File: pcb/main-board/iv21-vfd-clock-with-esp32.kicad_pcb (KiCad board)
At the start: 2 copper layers, 101.5 x 40 mm, 29 parts, among them J1 Conn_02x10_Odd_Even, J2 4328, P1 USB_C_Plug_USB2.0, SW1 SW_SPST, SW2 SW_SPST, U1 MAX6921AQI_, U2 MOUDLE-SEEEDUINO-XIAO-ESP32C3, U3 AP3012, U4 S-1167B24-M5T

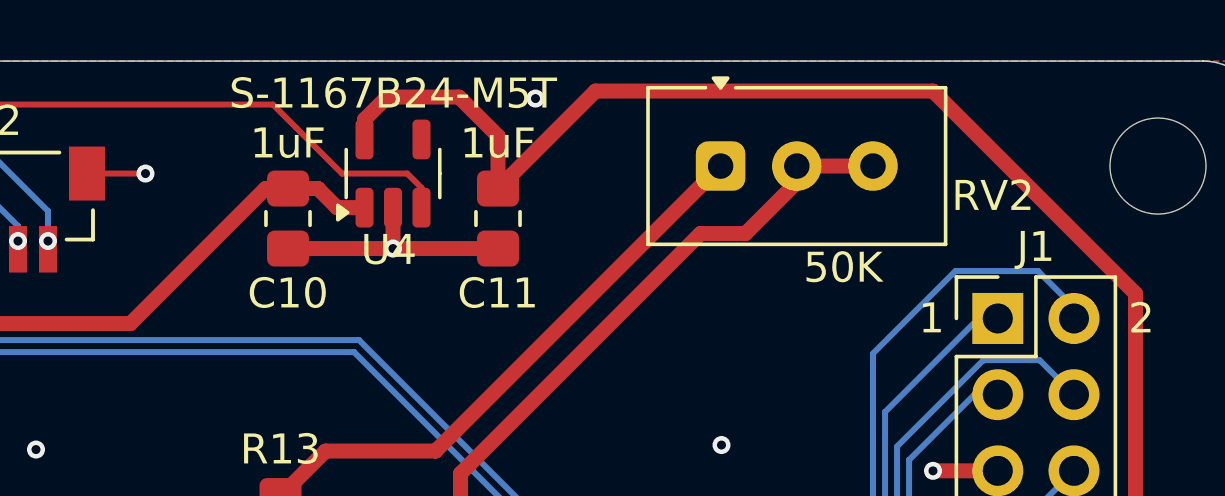
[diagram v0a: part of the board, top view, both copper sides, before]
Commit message: Fix some silkmask labels for trim pot.
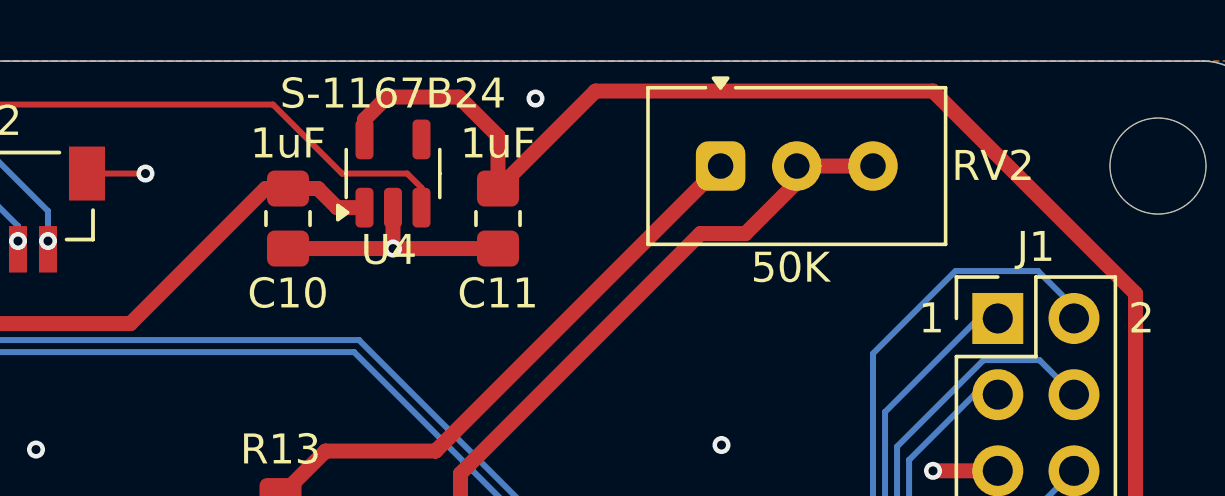
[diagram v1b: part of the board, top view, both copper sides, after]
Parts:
- U4: value S-1167B24-M5T -> S-1167B24
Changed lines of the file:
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@@
 		(tags "Potentiometer horizontal vishay")
 		(property "Reference" "RV2"
-			(at 9.08 1 0)
+			(at 9.08 0 0)
 			(layer "F.SilkS")
 			(effects
@@
 		)
 		(property "Value" "50K"
-			(at 4.08 3.3925 0)
+			(at 2.33 3.3925 0)
 			(unlocked yes)
 			(layer "F.SilkS")
@@
 			)
 		)
-		(property "Value" "S-1167B24-M5T"
+		(property "Value" "S-1167B24"
 			(at 2.6625 0 0)
 			(layer "F.SilkS")

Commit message: ...
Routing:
- net GND: track 37.3 -> 34.0 mm, vias 20 -> 18
- net /5V: track 135.4 -> 132.3 mm, vias 2 -> 0
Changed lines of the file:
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@@
-	)
-	(segment
-		(start 76.6605 42.2105)
-		(end 76.7 42.25)
-		(width 0.2)
-		(layer "F.Cu")
-		(net 11)
-	)
-	(segment
-		(start 94 39)
-		(end 90.75 42.25)
-		(width 0.65)
-		(layer "F.Cu")
-		(net 11)
 	)
 	(segment
@@
 	)
 	(segment
+		(start 77.75 42.3)
+		(end 77.7 42.25)
+		(width 0.2)
+		(layer "F.Cu")
+		(net 11)
+	)
+	(segment
 		(start 90.75 42.25)
-		(end 77.7 42.25)
+		(end 94 39)
 		(width 0.65)
 		(layer "F.Cu")
@@
 	)
 	(segment
-		(start 46.93 25.355)
-		(end 46.93 24.4)
-		(width 0.3)
+		(start 79 23.34)
+		(end 77 25.34)
+		(width 0.5)
+		(layer "F.Cu")
+		(net 11)
+	)
+	(segment
+		(start 79.75 51)
+		(end 79.75 53.5)
+		(width 0.65)
+		(layer "F.Cu")
+		(net 11)
+	)
+	(segment
+		(start 105.6375 22.8875)
+		(end 106.55 22.8875)
+		(width 0.5)
+		(layer "F.Cu")
+		(net 11)
+	)
+	(segment
+		(start 46.93 32.98)
+		(end 56.2 42.25)
+		(width 0.65)
+		(layer "F.Cu")
+		(net 11)
+	)
+	(segment
+		(start 105 22.25)
+		(end 105.6375 22.8875)
+		(width 0.5)
+		(layer "F.Cu")
+		(net 11)
+	)
+	(segment
+		(start 76.7 42.25)
+		(end 56.2 42.25)
+		(width 0.65)
+		(layer "F.Cu")
+		(net 11)
+	)
+	(segment
+		(start 80.5 54.25)
+		(end 86.0875 54.25)
+		(width 0.65)
 		(layer "F.Cu")
 		(net 11)
@@
 	)
 	(segment
-		(start 77.75 42.3)
-		(end 77.7 42.25)
-		(width 0.2)
-		(layer "F.Cu")
-		(net 11)
-	)
-	(segment
-		(start 79.75 51)
-		(end 79.75 53.5)
-		(width 0.65)
-		(layer "F.Cu")
-		(net 11)
-	)
-	(segment
-		(start 105.6375 22.8875)
-		(end 106.55 22.8875)
-		(width 0.5)
-		(layer "F.Cu")
-		(net 11)
-	)
-	(segment
-		(start 46.93 32.98)
-		(end 56.2 42.25)
-		(width 0.65)
-		(layer "F.Cu")
-		(net 11)
-	)
-	(segment
-		(start 77 41.871)
-		(end 76.6605 42.2105)
-		(width 0.5)
-		(layer "F.Cu")
-		(net 11)
-	)
-	(segment
-		(start 105 22.25)
-		(end 105.6375 22.8875)
-		(width 0.5)
-		(layer "F.Cu")
-		(net 11)
-	)
-	(segment
-		(start 76.7 42.25)
-		(end 56.2 42.25)
-		(width 0.65)
-		(layer "F.Cu")
-		(net 11)
-	)
-	(segment
-		(start 80.5 54.25)
-		(end 86.0875 54.25)
-		(width 0.65)
-		(layer "F.Cu")
-		(net 11)
-	)
-	(segment
 		(start 46.93 26.4)
 		(end 46.93 32.98)
@@
 	)
 	(segment
-		(start 77.7 42.25)
-		(end 76.7 42.25)
-		(width 0.65)
-		(layer "F.Cu")
-		(net 11)
-	)
-	(segment
 		(start 46.93 24.98666)
 		(end 46.901109 24.957769)
@@
 	)
 	(segment
-		(start 77 25.34)
-		(end 77 41.871)
-		(width 0.5)
+		(start 76.7 42.25)
+		(end 90.75 42.25)
+		(width 0.65)
 		(layer "F.Cu")
 		(net 11)
@@
 	)
 	(segment
-		(start 79 23.34)
-		(end 77 25.34)
+		(start 77 25.34)
+		(end 77 42.25)
 		(width 0.5)
 		(layer "F.Cu")
@@
 		(net 11)
 	)
-	(via
-		(at 46.93 24.4)
-		(size 0.6)
-		(drill 0.3)
-		(layers "F.Cu" "B.Cu")
-		(free yes)
-		(net 11)
-	)
-	(via
-		(at 46.93 26.4)
-		(size 0.6)
-		(drill 0.3)
-		(layers "F.Cu" "B.Cu")
-		(net 11)
-	)
-	(segment
-		(start 46.93 24.4)
-		(end 46.93 26.4)
-		(width 0.65)
-		(layer "B.Cu")
-		(net 11)
-	)
 	(segment
 		(start 60.599 23.499)
@@
 	)
 	(segment
-		(start 45.48 25.355)
-		(end 45.48 27)
-		(width 0.2)
-		(layer "F.Cu")
-		(net 38)
-	)
-	(segment
-		(start 51.88 25.355)
-		(end 51.88 27)
-		(width 0.2)
-		(layer "F.Cu")
-		(net 38)
-	)
-	(segment
 		(start 103.75 44.5)
 		(end 103.75 41.75)
@@
 	)
 	(via
-		(at 51.88 27)
-		(size 0.6)
-		(drill 0.3)
-		(layers "F.Cu" "B.Cu")
-		(net 38)
-	)
-	(via
 		(at 43.5 37.5)
 		(size 0.6)
@@
 		(layers "F.Cu" "B.Cu")
 		(free yes)
-		(net 38)
-	)
-	(via
-		(at 45.48 27)
-		(size 0.6)
-		(drill 0.3)
-		(layers "F.Cu" "B.Cu")
 		(net 38)
 	)
@@
 			(pts
 				(xy 46.93 26.35) (xy 47.25 26.35) (xy 46.930194 25.15) (xy 46.609748 26.349661)
+			)
+		)
+	)
+	(zone
+		(net 38)
+		(net_name "GND")
+		(layer "F.Cu")
+		(hatch edge 0.5)
+		(priority 2)
+		(connect_pads
+			(clearance 0)
+		)
+		(min_thickness 0.25)
+		(filled_areas_thickness no)
+		(fill yes
+			(thermal_gap 0.5)
+			(thermal_bridge_width 0.5)
+		)
+		(polygon
+			(pts
+				(xy 51.65 25.85) (xy 51.65 26.45) (xy 52.15 26.45) (xy 52.15 25.85)
 			)
 		)
@@
 			)
 		)
+	)
+	(zone
+		(net 38)
+		(net_name "GND")
+		(layer "F.Cu")
+		(hatch edge 0.5)
+		(priority 2)
+		(connect_pads
+			(clearance 0)
+		)
+		(min_thickness 0.25)
+		(filled_areas_thickness no)
+		(fill yes
+			(thermal_gap 0.5)
+			(thermal_bridge_width 0.5)
+		)
+		(polygon
+			(pts
+				(xy 45.25 25.85) (xy 45.25 26.45) (xy 45.75 26.45) (xy 45.75 25.85)
+			)
+		)

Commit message: ...
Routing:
- net /5V: track 132.3 -> 137.1 mm
- net GND: track 34.0 -> 37.2 mm, vias 18 -> 21
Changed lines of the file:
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@@
+	)
+	(segment
+		(start 78 42.25)
+		(end 77.75 42.25)
+		(width 0.65)
+		(layer "F.Cu")
+		(net 11)
 	)
 	(segment
@@
 	)
 	(segment
-		(start 77.75 42.3)
-		(end 77.7 42.25)
-		(width 0.2)
+		(start 77.75 50.5)
+		(end 77 49.75)
+		(width 0.65)
+		(layer "F.Cu")
+		(net 11)
+	)
+	(segment
+		(start 77.75 42.25)
+		(end 77 43)
+		(width 0.65)
+		(layer "F.Cu")
+		(net 11)
+	)
+	(segment
+		(start 79 23.34)
+		(end 77 25.34)
+		(width 0.65)
 		(layer "F.Cu")
 		(net 11)
@@
 	)
 	(segment
-		(start 79 23.34)
-		(end 77 25.34)
-		(width 0.5)
+		(start 77 43)
+		(end 76.25 42.25)
+		(width 0.65)
+		(layer "F.Cu")
+		(net 11)
+	)
+	(segment
+		(start 77 41.5)
+		(end 77 42.25)
+		(width 0.65)
 		(layer "F.Cu")
 		(net 11)
@@
 	(segment
 		(start 76.7 42.25)
-		(end 56.2 42.25)
+		(end 76.5 42.25)
 		(width 0.65)
 		(layer "F.Cu")
@@
 	)
 	(segment
-		(start 77.75 50.5)
-		(end 77.75 42.3)
-		(width 0.65)
-		(layer "F.Cu")
-		(net 11)
-	)
-	(segment
 		(start 46.93 26.4)
 		(end 46.93 32.98)
@@
 	)
 	(segment
+		(start 78 42.25)
+		(end 90.75 42.25)
+		(width 0.65)
+		(layer "F.Cu")
+		(net 11)
+	)
+	(segment
+		(start 77.75 42.25)
+		(end 77 41.5)
+		(width 0.65)
+		(layer "F.Cu")
+		(net 11)
+	)
+	(segment
 		(start 46.93 24.98666)
 		(end 46.901109 24.957769)
@@
 	)
 	(segment
+		(start 77 49.75)
+		(end 77 43)
+		(width 0.65)
+		(layer "F.Cu")
+		(net 11)
+	)
+	(segment
 		(start 103.25 22.25)
 		(end 104 22.25)
@@
 	(segment
 		(start 76.7 42.25)
-		(end 90.75 42.25)
+		(end 78 42.25)
+		(width 0.65)
+		(layer "F.Cu")
+		(net 11)
+	)
+	(segment
+		(start 76.5 42.25)
+		(end 56.2 42.25)
 		(width 0.65)
 		(layer "F.Cu")
@@
 	)
 	(segment
-		(start 77 25.34)
-		(end 77 42.25)
-		(width 0.5)
-		(layer "F.Cu")
-		(net 11)
-	)
-	(segment
 		(start 79.75 53.5)
 		(end 80.5 54.25)
@@
 	)
 	(segment
+		(start 77 41.5)
+		(end 76.25 42.25)
+		(width 0.65)
+		(layer "F.Cu")
+		(net 11)
+	)
+	(segment
+		(start 77 25.34)
+		(end 77 41.5)
+		(width 0.65)
+		(layer "F.Cu")
+		(net 11)
+	)
+	(segment
+		(start 77 43)
+		(end 77 42.25)
+		(width 0.65)
+		(layer "F.Cu")
+		(net 11)
+	)
+	(segment
 		(start 79 23.34)
 		(end 80.09 23.34)
@@
 	)
 	(segment
+		(start 108.35 24.25)
+		(end 106.65 24.25)
+		(width 0.5)
+		(layer "F.Cu")
+		(net 38)
+	)
+	(segment
 		(start 115 48)
 		(end 114.729999 48.270001)
@@
 	)
 	(segment
+		(start 103.75 44.5)
+		(end 103.75 41.75)
+		(width 0.5)
+		(layer "F.Cu")
+		(net 38)
+	)
+	(segment
+		(start 108.35 24.25)
+		(end 107.5 25.1)
+		(width 0.5)
+		(layer "F.Cu")
+		(net 38)
+	)
+	(segment
 		(start 87 48.25)
 		(end 87 50.1125)
@@
 	)
 	(segment
-		(start 103.75 44.5)
-		(end 103.75 41.75)
+		(start 111 24.25)
+		(end 108.35 24.25)
+		(width 0.5)
+		(layer "F.Cu")
+		(net 38)
+	)
+	(segment
+		(start 104 24.25)
+		(end 106.65 24.25)
 		(width 0.5)
 		(layer "F.Cu")
@@
 	)
 	(segment
-		(start 107.5 24.25)
+		(start 107.5 25.1)
 		(end 107.5 22.8875)
 		(width 0.5)
@@
 	)
 	(segment
-		(start 111 24.25)
-		(end 107.5 24.25)
-		(width 0.5)
-		(layer "F.Cu")
-		(net 38)
-	)
-	(segment
 		(start 127.66 36.74)
 		(end 126.76 36.74)
@@
 	)
 	(segment
-		(start 104 24.25)
-		(end 107.5 24.25)
+		(start 106.65 24.25)
+		(end 107.5 25.1)
 		(width 0.5)
 		(layer "F.Cu")
@@
 	)
 	(via
-		(at 107.5 24.25)
+		(at 107.5 25.1)
 		(size 0.6)
 		(drill 0.3)
@@
 	)
 	(via
+		(at 51.88 27.5)
+		(size 0.6)
+		(drill 0.3)
+		(layers "F.Cu" "B.Cu")
+		(net 38)
+	)
+	(via
 		(at 91.2 24.6)
 		(size 0.6)
@@
 	)
 	(via
+		(at 45.48 27.5)
+		(size 0.6)
+		(drill 0.3)
+		(layers "F.Cu" "B.Cu")
+		(net 38)
+	)
+	(via
 		(at 125.5 31.66)
 		(size 0.6)
@@
 	(via
 		(at 83.425 28.4)
+		(size 0.6)
+		(drill 0.3)
+		(layers "F.Cu" "B.Cu")
+		(free yes)
+		(net 38)
+	)
+	(via
+		(at 105.35 19.15)
 		(size 0.6)
 		(drill 0.3)
@@
 		(layer "F.Cu")
 		(hatch edge 0.5)
-		(priority 2)
-		(connect_pads
+		(priority 1)
+		(connect_pads yes
 			(clearance 0)
 		)
@@
 		(polygon
 			(pts
-				(xy 51.65 25.85) (xy 51.65 26.45) (xy 52.15 26.45) (xy 52.15 25.85)
+				(xy 51.65 25.85) (xy 51.35 26.65) (xy 52.45 26.65) (xy 52.15 25.85)
 			)
 		)
@@
 		(hatch edge 0.5)
 		(priority 2)
-		(connect_pads
+		(connect_pads yes
 			(clearance 0)
 		)
@@
 		(polygon
 			(pts
-				(xy 45.25 25.85) (xy 45.25 26.45) (xy 45.75 26.45) (xy 45.75 25.85)
+				(xy 45.25 25.85) (xy 44.95 26.65) (xy 46.05 26.65) (xy 45.75 25.85)
 			)
 		)
@@
 		(polygon
 			(pts
-				(xy 110.2 24.771753) (xy 104.8 24.771753) (xy 104.8 23.621753) (xy 110.2 23.671753)
+				(xy 110.2 24.721753) (xy 104.8 24.721753) (xy 104.8 23.621753) (xy 110.2 23.671753)
 			)
 		)

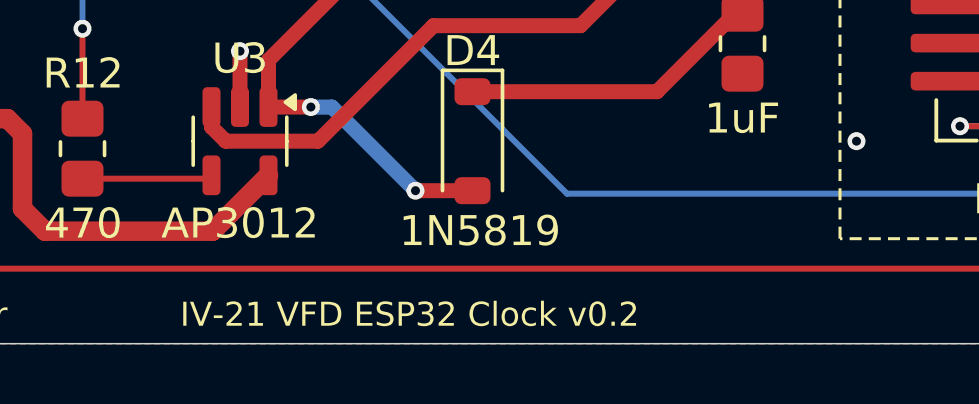
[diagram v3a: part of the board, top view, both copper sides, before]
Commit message: Update silkscreen labels to say v0.3
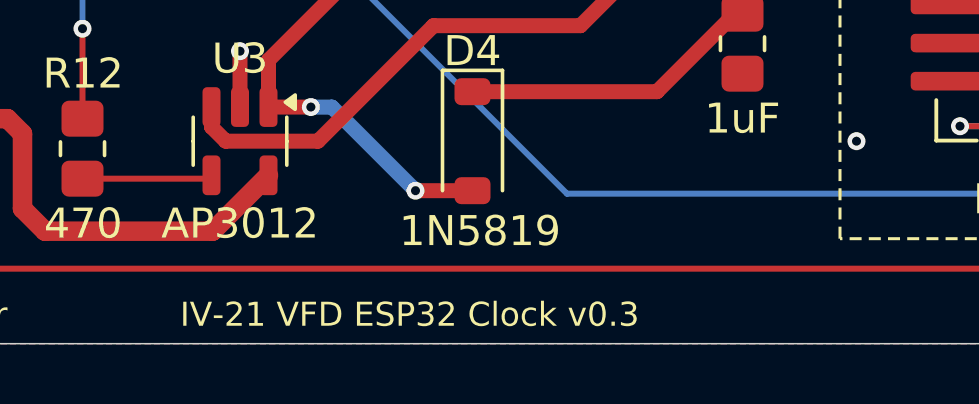
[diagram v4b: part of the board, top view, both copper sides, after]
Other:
- board text added: "IV-21 VFD ESP32 Clock v0.3"
- board text removed: "IV-21 VFD ESP32 Clock v0.2"
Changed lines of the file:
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@@
 		)
 	)
-	(gr_text "IV-21 VFD ESP32 Clock v0.2"
+	(gr_text "IV-21 VFD ESP32 Clock v0.3"
 		(at 85 57.5 0)
 		(layer "F.SilkS")
